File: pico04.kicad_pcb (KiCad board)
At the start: 2 copper layers, 38.2 x 41.8 mm, 33 parts, among them SW1 SW_Push, U1 PRTR5V0U2X, U2 ATmega16U2-MU, Y1 16MHz

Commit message: Complete the PCB
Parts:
- moved F1 8.51 mm to (96.5, 62.8), turned to 180 degrees
- moved R4 6.99 mm to (99.0, 58.8)
- moved R5 5.53 mm to (97.1, 58.8)
- moved U1 5.13 mm to (95.7, 54.7), turned to 90 degrees
- moved R2 2.71 mm to (100.4, 54.9)
- moved R1 0.49 mm to (91.3, 54.9)
- renumbered D3 to D1, D4 to D2, D1 to D3, D2 to D4, MX3 to MX1, MX4 to MX2, MX1 to MX3, MX2 to MX4
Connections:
- D1 pad 1: ROW1 -> ROW0
- D2 pad 1: ROW1 -> ROW0
- D3 pad 1: ROW0 -> ROW1
- D4 pad 1: ROW0 -> ROW1
- U2 pad 16: Net-(U2-Pad16) -> ROW1
- U2 pad 22: Net-(U2-Pad22) -> COL0
- U2 pad 25: Net-(U2-Pad25) -> ROW0
- U2 pad 9: Net-(U2-Pad9) -> COL1
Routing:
- net GND: track 13.2 -> 184.5 mm
- net +5V: track 0.00 -> 140.1 mm, vias 0 -> 3
- net COL1: track 0.00 -> 37.3 mm, vias 0 -> 2
- net Net-(RGB2-Pad2): track 0.00 -> 35.5 mm, vias 0 -> 2
- net COL0: track 0.00 -> 31.0 mm, vias 0 -> 2
- net XTAL2: track 0.00 -> 23.3 mm, vias 0 -> 2
- net ROW0: track 0.00 -> 22.7 mm, vias 0 -> 2
- net Net-(R3-Pad2): track 0.00 -> 22.2 mm, vias 0 -> 2
- net XTAL1: track 0.00 -> 17.2 mm
- net RGBLED: track 0.00 -> 16.8 mm, vias 0 -> 2
- net Net-(R4-Pad2): track 0.00 -> 16.8 mm, vias 0 -> 2
- net VCC: track 7.28 -> 23.6 mm, vias 0 -> 4
- net Net-(RGB3-Pad2): track 0.00 -> 14.5 mm, vias 0 -> 2
- net Net-(RGB1-Pad2): track 0.00 -> 14.5 mm, vias 0 -> 2
- net Net-(R5-Pad2): track 0.00 -> 13.3 mm, vias 0 -> 2
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
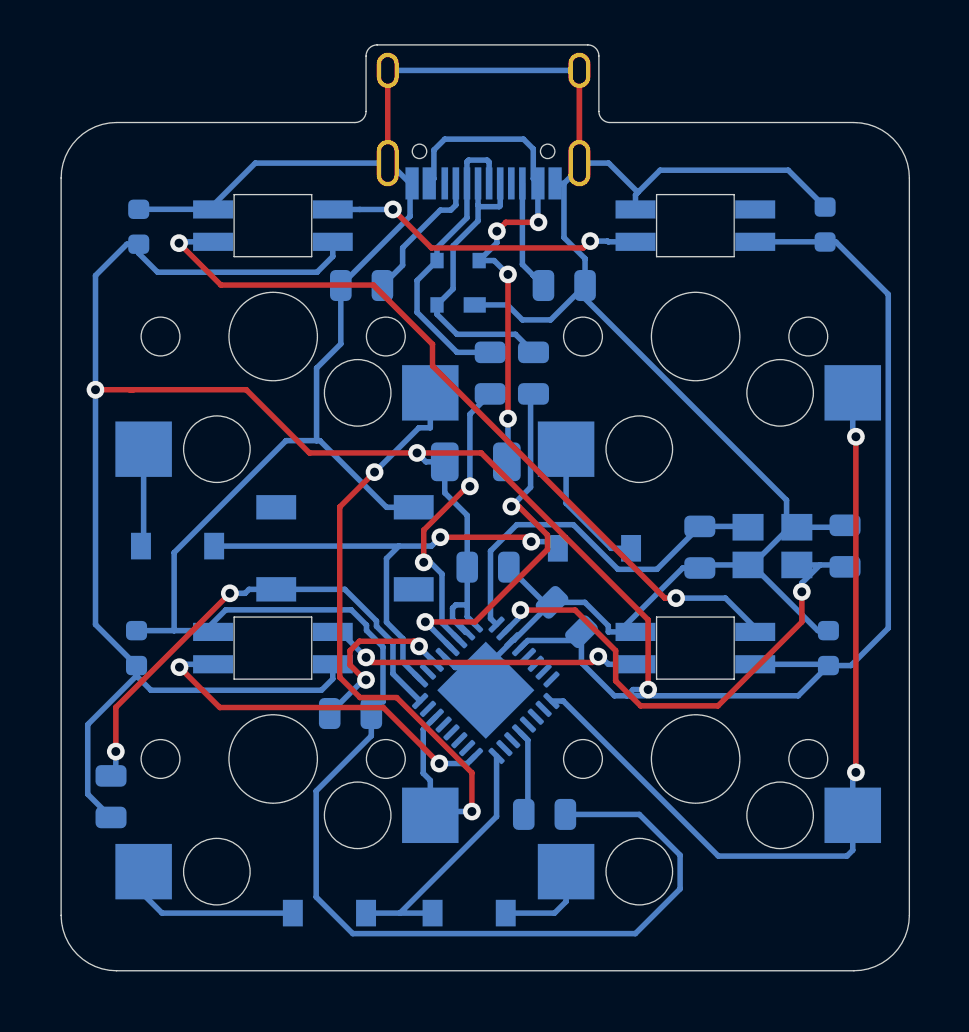
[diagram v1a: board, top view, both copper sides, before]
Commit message: Add some 3d models to the PCB
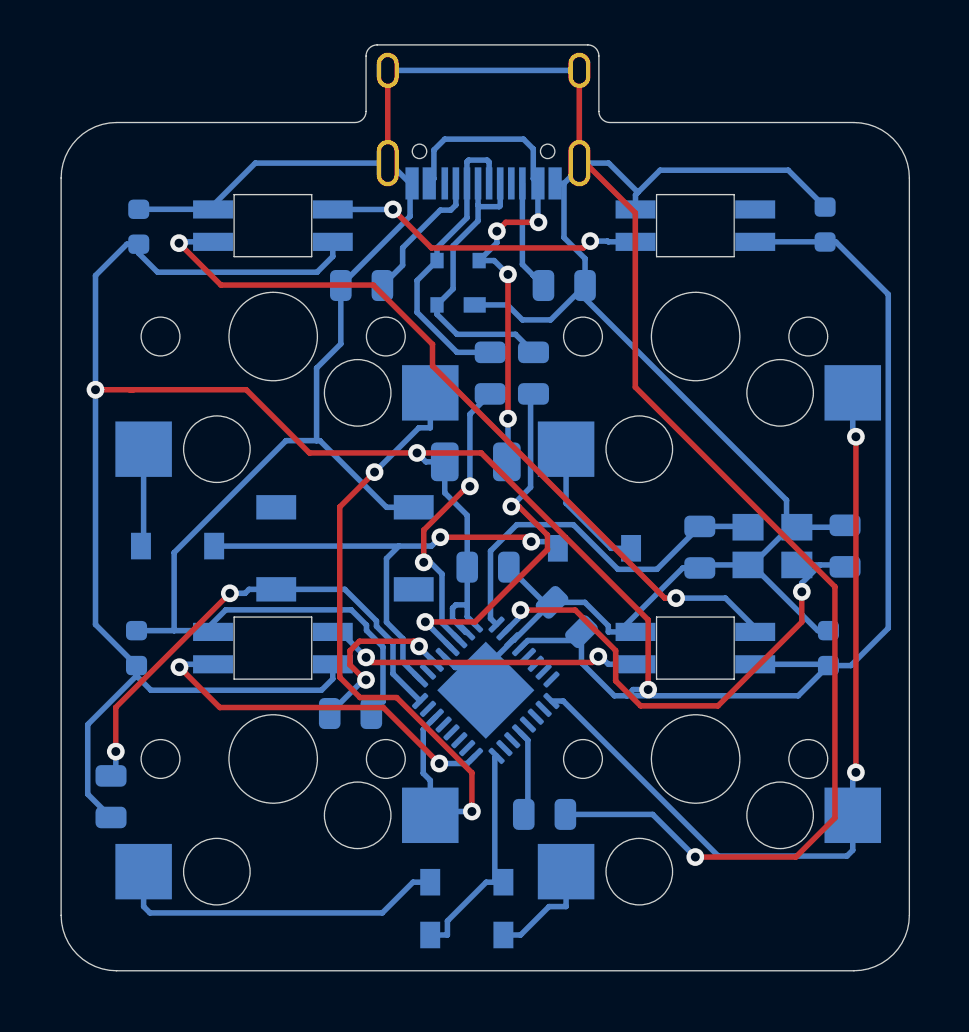
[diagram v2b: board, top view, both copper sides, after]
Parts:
- USB1: footprint Type-C:HRO-TYPE-C-31-M-12 -> Pico04:HRO-TYPE-C-31-M-12
- moved D3 6.35 mm to (96.0, 81.8)
- moved D4 0.99 mm to (96.0, 84.1)
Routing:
- net GND: track 184.5 -> 198.1 mm, vias 0 -> 1
- net Net-(D3-Pad2): track 8.11 -> 15.2 mm
- net ROW1: track 11.9 -> 10.4 mm
- net COL0: track 31.0 -> 31.7 mm
- net Net-(D4-Pad2): track 4.29 -> 4.93 mm

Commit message: Fix 3d model issues
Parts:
- F1: footprint Fuse:Fuse_1206_3216Metric -> Pico04:Fuse_1206_3216Metric
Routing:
- added copper zone on B.Cu, net (none)
- added copper zone on F.Cu, net (none)
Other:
- board text added: "Pico04 v01"
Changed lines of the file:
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@@
   (general
     (thickness 1.6)
-    (drawings 32)
+    (drawings 33)
     (tracks 404)
     (modules 33)
@@
     (add_net "XTAL2")
   )
+  (module "Pico04:Fuse_1206_3216Metric" (layer "B.Cu")
+    (at 96.45 62.8 180)
+    (descr "Fuse SMD 1206 (3216 Metric), square (rectangular) end terminal, IPC_7351 nominal, (Body size source: http://www.tortai-tech.com/upload/download/2011102023233369053.pdf), generated with kicad-footprint-generator")
+    (tags "resistor")
+    (attr smd)
+    (fp_text reference "F1" (at 0 1.82) (layer "B.SilkS")
+      (effects (font (size 1 1) (thickness 0.15)) (justify mirror))
+    )
+    (fp_text value "500mA" (at 0 -1.82) (layer "B.Fab")
+      (effects (font (size 1 1) (thickness 0.15)) (justify mirror))
+    )
+    (fp_text user "${REFERENCE}" (at 0 0) (layer "B.Fab")
+      (effects (font (size 0.8 0.8) (thickness 0.12)) (justify mirror))
+    )
+    (fp_line (start 2.28 -1.12) (end -2.28 -1.12) (layer "B.CrtYd") (width 0.05))
+    (fp_line (start 2.28 1.12) (end 2.28 -1.12) (layer "B.CrtYd") (width 0.05))
+    (fp_line (start -2.28 1.12) (end 2.28 1.12) (layer "B.CrtYd") (width 0.05))
+    (fp_line (start -2.28 -1.12) (end -2.28 1.12) (layer "B.CrtYd") (width 0.05))
+    (fp_line (start -0.602064 -0.91) (end 0.602064 -0.91) (layer "B.SilkS") (width 0.12))
+    (fp_line (start -0.602064 0.91) (end 0.602064 0.91) (layer "B.SilkS") (width 0.12))
+    (fp_line (start 1.6 -0.8) (end -1.6 -0.8) (layer "B.Fab") (width 0.1))
+    (fp_line (start 1.6 0.8) (end 1.6 -0.8) (layer "B.Fab") (width 0.1))
+    (fp_line (start -1.6 0.8) (end 1.6 0.8) (layer "B.Fab") (width 0.1))
+    (fp_line (start -1.6 -0.8) (end -1.6 0.8) (layer "B.Fab") (width 0.1))
+    (pad "2" smd roundrect (at 1.4 0 180) (size 1.25 1.75) (layers "B.Cu" "B.Paste" "B.Mask") (roundrect_rratio 0.2)
+      (net 3 "+5V"))
+    (pad "1" smd roundrect (at -1.4 0 180) (size 1.25 1.75) (layers "B.Cu" "B.Paste" "B.Mask") (roundrect_rratio 0.2)
+      (net 12 "VCC"))
+    (model "${KISYS3DMOD}/Fuse.3dshapes/Fuse_1206_3216Metric.wrl"
+      (at (xyz 0 0 0))
+      (scale (xyz 1 1 1))
+      (rotate (xyz 0 0 0))
+    )
+    (model "${KIPRJMOD}/3d models/0ZCJ0050AF2E.step"
+      (at (xyz 0 0 0))
+      (scale (xyz 1 1 1))
+      (rotate (xyz 0 0 0))
+    )
+  )
   (module "Pico04:HRO-TYPE-C-31-M-12" (layer "B.Cu")
     (at 96.8 42.55)
@@
     (pad "4" smd rect (at -2.7 0.73) (size 1.8 0.82) (layers "B.Cu" "B.Paste" "B.Mask")
       (net 26 "Net-(RGB3-Pad2)") (pinfunction "DIN"))
+    (model "${KIPRJMOD}/3d models/WS2812_RGB_LED.stp"
+      (at (xyz 0 0 0))
+      (scale (xyz 1 1 1))
+      (rotate (xyz 0 0 90))
+    )
   )
   (module "Pico04:WS2812B-3528" (layer "B.Cu")
@@
     (pad "4" smd rect (at -2.7 0.73) (size 1.8 0.82) (layers "B.Cu" "B.Paste" "B.Mask")
       (net 25 "Net-(RGB2-Pad2)") (pinfunction "DIN"))
+    (model "${KIPRJMOD}/3d models/WS2812_RGB_LED.stp"
+      (at (xyz 0 0 0))
+      (scale (xyz 1 1 1))
+      (rotate (xyz 0 0 90))
+    )
   )
   (module "Pico04:WS2812B-3528" (layer "B.Cu")
@@
     (pad "4" smd rect (at -2.7 0.73) (size 1.8 0.82) (layers "B.Cu" "B.Paste" "B.Mask")
       (net 23 "Net-(RGB1-Pad2)") (pinfunction "DIN"))
+    (model "${KIPRJMOD}/3d models/WS2812_RGB_LED.stp"
+      (at (xyz 0 0 0))
+      (scale (xyz 1 1 1))
+      (rotate (xyz 0 0 90))
+    )
   )
   (module "Pico04:WS2812B-3528" (layer "B.Cu")
@@
     (pad "4" smd rect (at -2.7 0.73) (size 1.8 0.82) (layers "B.Cu" "B.Paste" "B.Mask")
       (net 24 "RGBLED") (pinfunction "DIN"))
+    (model "${KIPRJMOD}/3d models/WS2812_RGB_LED.stp"
+      (at (xyz 0 0 0))
+      (scale (xyz 1 1 1))
+      (rotate (xyz 0 0 90))
+    )
   )
   (module "Crystal:Crystal_SMD_3225-4Pin_3.2x2.5mm" (layer "B.Cu")
@@
     )
   )
-  (module "Fuse:Fuse_1206_3216Metric" (layer "B.Cu")
-    (at 96.45 62.8 180)
-    (descr "Fuse SMD 1206 (3216 Metric), square (rectangular) end terminal, IPC_7351 nominal, (Body size source: http://www.tortai-tech.com/upload/download/2011102023233369053.pdf), generated with kicad-footprint-generator")
-    (tags "resistor")
-    (attr smd)
-    (fp_text reference "F1" (at -1.15 -2) (layer "B.SilkS")
-      (effects (font (size 1 1) (thickness 0.15)) (justify mirror))
-    )
-    (fp_text value "500mA" (at 0 -1.82) (layer "B.Fab")
-      (effects (font (size 1 1) (thickness 0.15)) (justify mirror))
-    )
-    (fp_text user "${REFERENCE}" (at 0 0 270) (layer "B.Fab")
-      (effects (font (size 0.8 0.8) (thickness 0.12)) (justify mirror))
-    )
-    (fp_line (start 2.28 -1.12) (end -2.28 -1.12) (layer "B.CrtYd") (width 0.05))
-    (fp_line (start 2.28 1.12) (end 2.28 -1.12) (layer "B.CrtYd") (width 0.05))
-    (fp_line (start -2.28 1.12) (end 2.28 1.12) (layer "B.CrtYd") (width 0.05))
-    (fp_line (start -2.28 -1.12) (end -2.28 1.12) (layer "B.CrtYd") (width 0.05))
-    (fp_line (start -0.602064 -0.91) (end 0.602064 -0.91) (layer "B.SilkS") (width 0.12))
-    (fp_line (start -0.602064 0.91) (end 0.602064 0.91) (layer "B.SilkS") (width 0.12))
-    (fp_line (start 1.6 -0.8) (end -1.6 -0.8) (layer "B.Fab") (width 0.1))
-    (fp_line (start 1.6 0.8) (end 1.6 -0.8) (layer "B.Fab") (width 0.1))
-    (fp_line (start -1.6 0.8) (end 1.6 0.8) (layer "B.Fab") (width 0.1))
-    (fp_line (start -1.6 -0.8) (end -1.6 0.8) (layer "B.Fab") (width 0.1))
-    (pad "2" smd roundrect (at 1.4 0 180) (size 1.25 1.75) (layers "B.Cu" "B.Paste" "B.Mask") (roundrect_rratio 0.2)
-      (net 3 "+5V"))
-    (pad "1" smd roundrect (at -1.4 0 180) (size 1.25 1.75) (layers "B.Cu" "B.Paste" "B.Mask") (roundrect_rratio 0.2)
-      (net 12 "VCC"))
-    (model "${KISYS3DMOD}/Fuse.3dshapes/Fuse_1206_3216Metric.wrl"
-      (at (xyz 0 0 0))
-      (scale (xyz 1 1 1))
-      (rotate (xyz 0 0 0))
-    )
-  )
   (module "Diode_SMD:D_SOD-123" (layer "B.Cu")
     (at 101.8 66.7)
@@
       (rotate (xyz 0 0 0))
     )
+  )
+  (gr_text "Pico04 v01" (at 108.74375 84.1375) (layer "F.Cu")
+    (effects (font (size 1.5 1.5) (thickness 0.3)))
   )
   (gr_line (start 85.55 72.6) (end 85.55 69.8) (layer "Edge.Cuts") (width 0.05))
@@
   (segment (start 103.6429 51.5771) (end 103.6429 59.4344) (width 0.25) (layer "F.Cu") (net 1))
   (segment (start 101.12 49.0542) (end 103.6429 51.5771) (width 0.25) (layer "F.Cu") (net 1))
+  (zone (net 0) (net_name "") (layer "F.Cu") (hatch edge 0.508)
+    (connect_pads (clearance 0.508))
+    (min_thickness 0.254)
+    (fill yes (thermal_gap 0.508) (thermal_bridge_width 0.508))
+    (polygon
+      (pts
+        (xy 116.68125 86.51875) (xy 76.99375 86.51875) (xy 76.99375 46.83125) (xy 116.68125 46.83125)
+      )
+    )
+  )
+  (zone (net 0) (net_name "") (layer "B.Cu") (hatch edge 0.508)
+    (connect_pads (clearance 0.508))
+    (min_thickness 0.254)
+    (fill yes (thermal_gap 0.508) (thermal_bridge_width 0.508))
+    (polygon
+      (pts
+        (xy 116.68125 86.51875) (xy 76.99375 86.51875) (xy 76.99375 46.83125) (xy 116.68125 46.83125)
+      )
+    )
+  )
 )

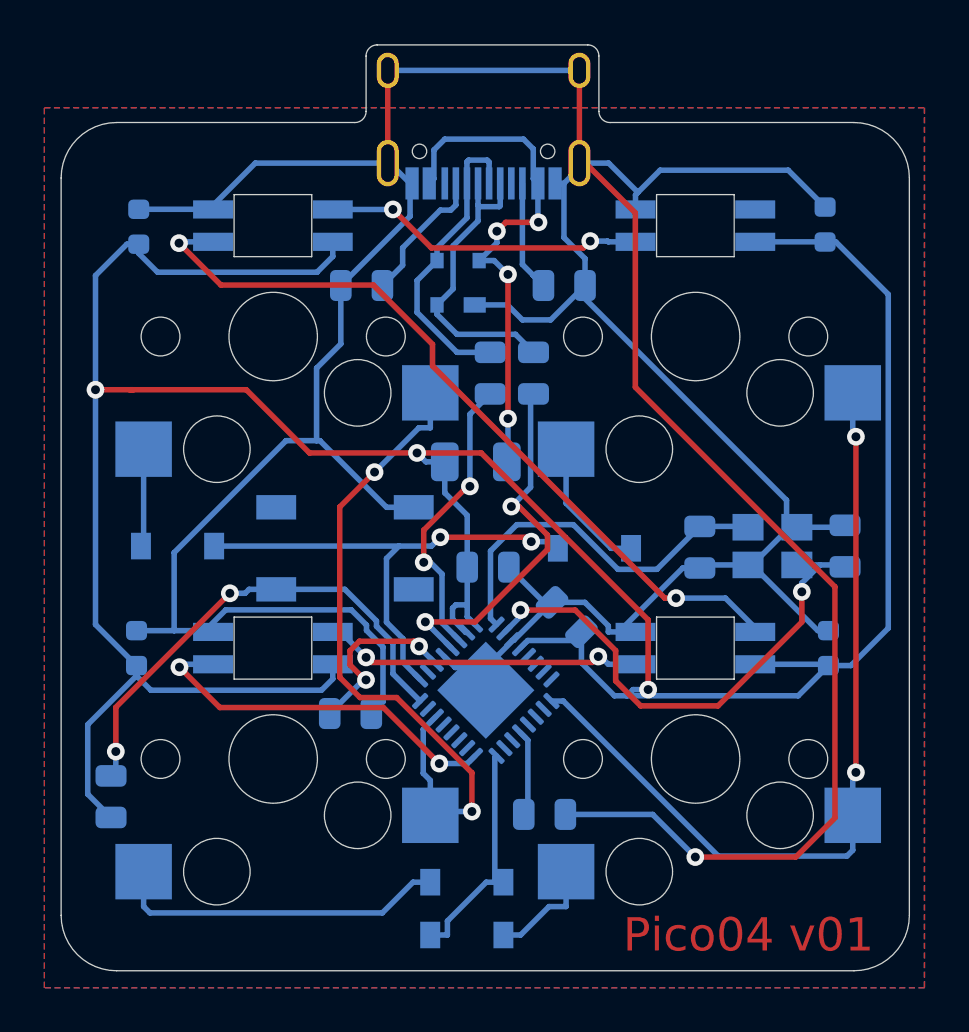
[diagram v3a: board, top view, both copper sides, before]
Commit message: Re-route the PCB
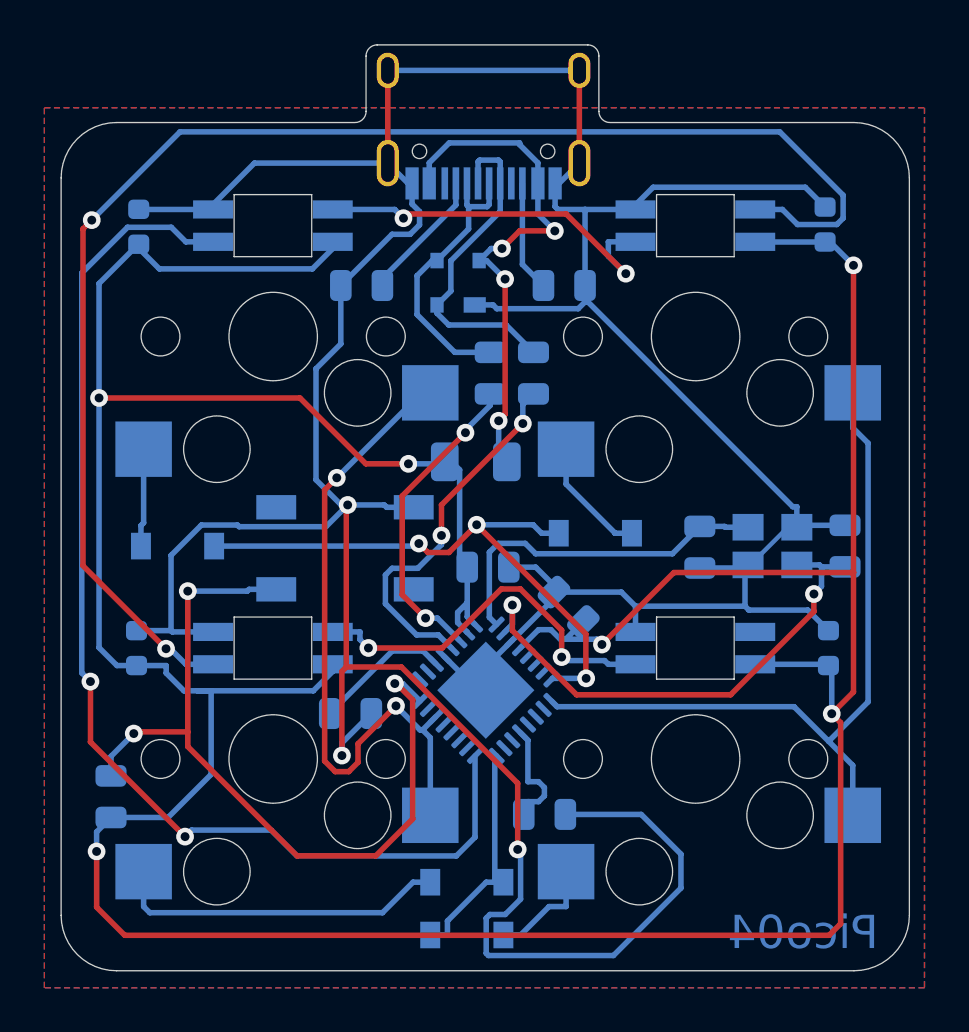
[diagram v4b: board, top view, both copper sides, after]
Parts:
- moved D2 0.68 mm to (101.8, 66.0)
- moved C3 0.47 mm to (100.6, 69.3)
- renumbered CRGB3 to CRGB1, CRGB1 to CRGB2, CRGB2 to CRGB3, RGB3 to RGB1, RGB4 to RGB2, RGB1 to RGB3, RGB2 to RGB4
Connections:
- RGB1 pad 4: Net-(RGB2-Pad2) -> RGBLED
- RGB2 pad 2: Net-(RGB4-Pad2) -> Net-(RGB2-Pad2)
- RGB3 pad 4: RGBLED -> Net-(RGB2-Pad2)
- RGB4 pad 2: Net-(RGB2-Pad2) -> Net-(RGB4-Pad2)
- U2 pad 25: ROW0 -> Net-(U2-Pad25)
- U2 pad 8: Net-(U2-Pad8) -> ROW0
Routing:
- net RGBLED: track 16.8 -> 52.1 mm
- net +5V: track 140.1 -> 174.7 mm, vias 3 -> 6
- net Net-(RGB2-Pad2): track 35.5 -> 65.6 mm
- net Net-(R3-Pad2): track 22.2 -> 36.7 mm, vias 2 -> 3
- net GND: track 198.1 -> 190.1 mm, vias 1 -> 3
- net ROW0: track 22.7 -> 27.0 mm, vias 2 -> 3
- net COL1: track 37.3 -> 33.8 mm, vias 2 -> 0
- net Net-(RGB1-Pad2): track 14.5 -> 17.6 mm
- net Net-(RGB3-Pad2): track 14.5 -> 17.4 mm
- net Net-(C1-Pad1): track 8.39 -> 6.19 mm, vias 2 -> 0
- net D+: track 13.8 -> 15.2 mm
- net COL0: track 31.7 -> 30.4 mm
- net XTAL1: track 17.2 -> 15.9 mm
- net Net-(R6-Pad1): track 3.92 -> 5.10 mm
- net Net-(R5-Pad2): track 13.3 -> 14.1 mm
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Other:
- board text added: "Pico04"
- board text removed: "Pico04 v01"

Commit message: Optimize some routing and update the images
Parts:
- turned R6 to 180 degrees
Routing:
- net GND: track 190.1 -> 165.6 mm
- net Net-(RGB1-Pad2): track 17.6 -> 16.2 mm
- net XTAL2: track 23.3 -> 24.3 mm
- net Net-(R6-Pad1): track 5.10 -> 4.54 mm
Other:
- outline, holes or cut-outs redrawn
